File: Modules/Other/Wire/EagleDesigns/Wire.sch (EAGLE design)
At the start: 2 parts

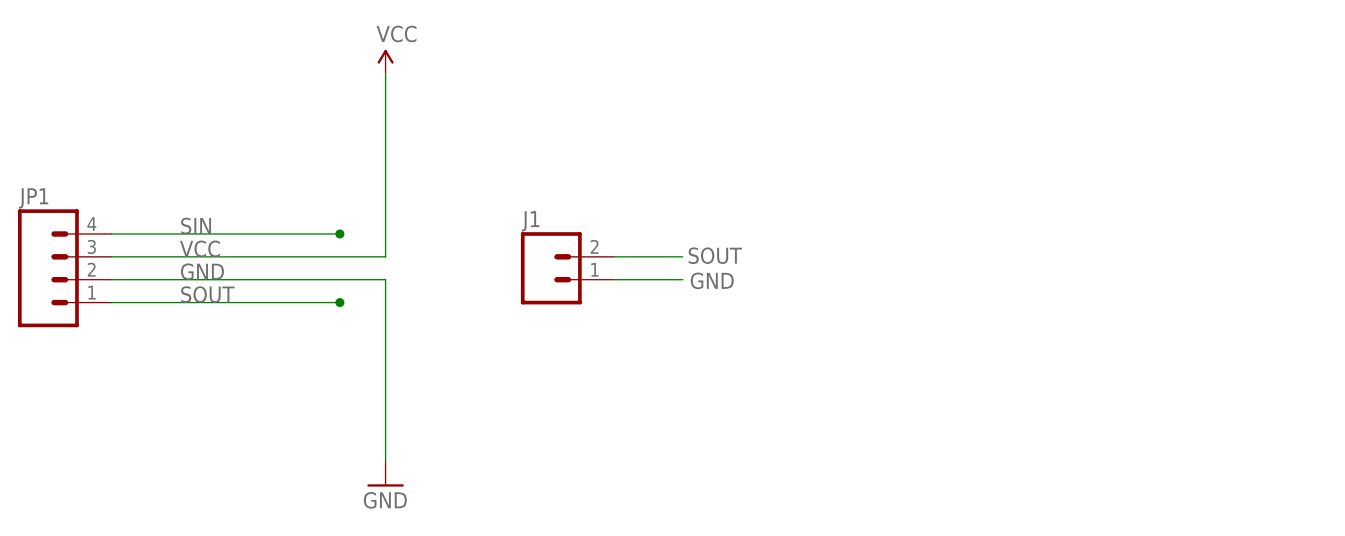
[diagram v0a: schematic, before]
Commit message: Added one single Board Layout for WireSEND, WireRECV, and Dummy module
it now has a small jumper that could be soldered in order to connect
SIN to SOUT.
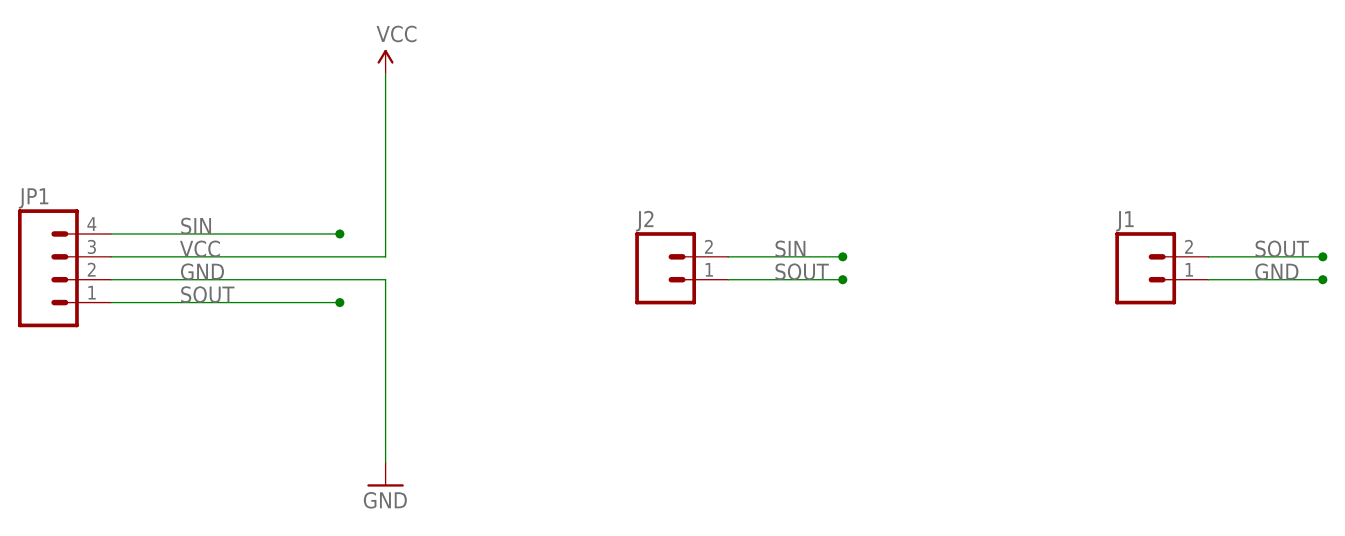
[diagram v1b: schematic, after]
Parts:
- added J2: (no value), SparkFun-Connectors:M02PTH
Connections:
- net SIN: now also J2.2
- net SOUT: now also J2.1
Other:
- moved on the sheet: J1
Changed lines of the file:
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@@
 <?xml version="1.0" encoding="utf-8"?>
 <!DOCTYPE eagle SYSTEM "eagle.dtd">
-<eagle version="7.6.0">
+<eagle version="7.3.0">
 <drawing>
 <settings>
@@
 <part name="SUPPLY1" library="SparkFun-Aesthetics" deviceset="VCC" device=""/>
 <part name="GND1" library="SparkFun-Aesthetics" deviceset="GND" device=""/>
+<part name="J2" library="SparkFun-Connectors" deviceset="M02" device="PTH"/>
 <part name="J1" library="SparkFun-Connectors" deviceset="M02" device="PTH"/>
 </parts>
@@
 <instance part="SUPPLY1" gate="G$1" x="40.64" y="27.94"/>
 <instance part="GND1" gate="1" x="40.64" y="-17.78"/>
-<instance part="J1" gate="G$1" x="58.42" y="5.08"/>
+<instance part="J2" gate="G$1" x="71.12" y="5.08"/>
+<instance part="J1" gate="G$1" x="124.46" y="5.08"/>
 </instances>
 <busses>
@@
 <segment>
 <pinref part="J1" gate="G$1" pin="1"/>
-<wire x1="66.04" y1="5.08" x2="73.66" y2="5.08" width="0.1524" layer="91"/>
-<label x="74.422" y="4.064" size="1.778" layer="95"/>
+<wire x1="132.08" y1="5.08" x2="144.78" y2="5.08" width="0.1524" layer="91"/>
+<junction x="144.78" y="5.08"/>
+<label x="137.16" y="5.08" size="1.778" layer="95"/>
 </segment>
 </net>
@@
 <junction x="35.56" y="10.16"/>
 </segment>
+<segment>
+<pinref part="J2" gate="G$1" pin="2"/>
+<wire x1="78.74" y1="7.62" x2="91.44" y2="7.62" width="0.1524" layer="91"/>
+<junction x="91.44" y="7.62"/>
+<label x="83.82" y="7.62" size="1.778" layer="95"/>
+</segment>
 </net>
 <net name="SOUT" class="0">
@@
 </segment>
 <segment>
+<pinref part="J2" gate="G$1" pin="1"/>
+<wire x1="78.74" y1="5.08" x2="91.44" y2="5.08" width="0.1524" layer="91"/>
+<junction x="91.44" y="5.08"/>
+<label x="83.82" y="5.08" size="1.778" layer="95"/>
+</segment>
+<segment>
 <pinref part="J1" gate="G$1" pin="2"/>
-<wire x1="66.04" y1="7.62" x2="73.66" y2="7.62" width="0.1524" layer="91"/>
-<label x="74.168" y="6.858" size="1.778" layer="95"/>
-</segment>
-</net>
+<wire x1="132.08" y1="7.62" x2="144.78" y2="7.62" width="0.1524" layer="91"/>
+<junction x="144.78" y="7.62"/>
+<label x="137.16" y="7.62" size="1.778" layer="95"/>
+</segment>
+</net>
